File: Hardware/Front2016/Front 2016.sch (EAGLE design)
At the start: 182 parts

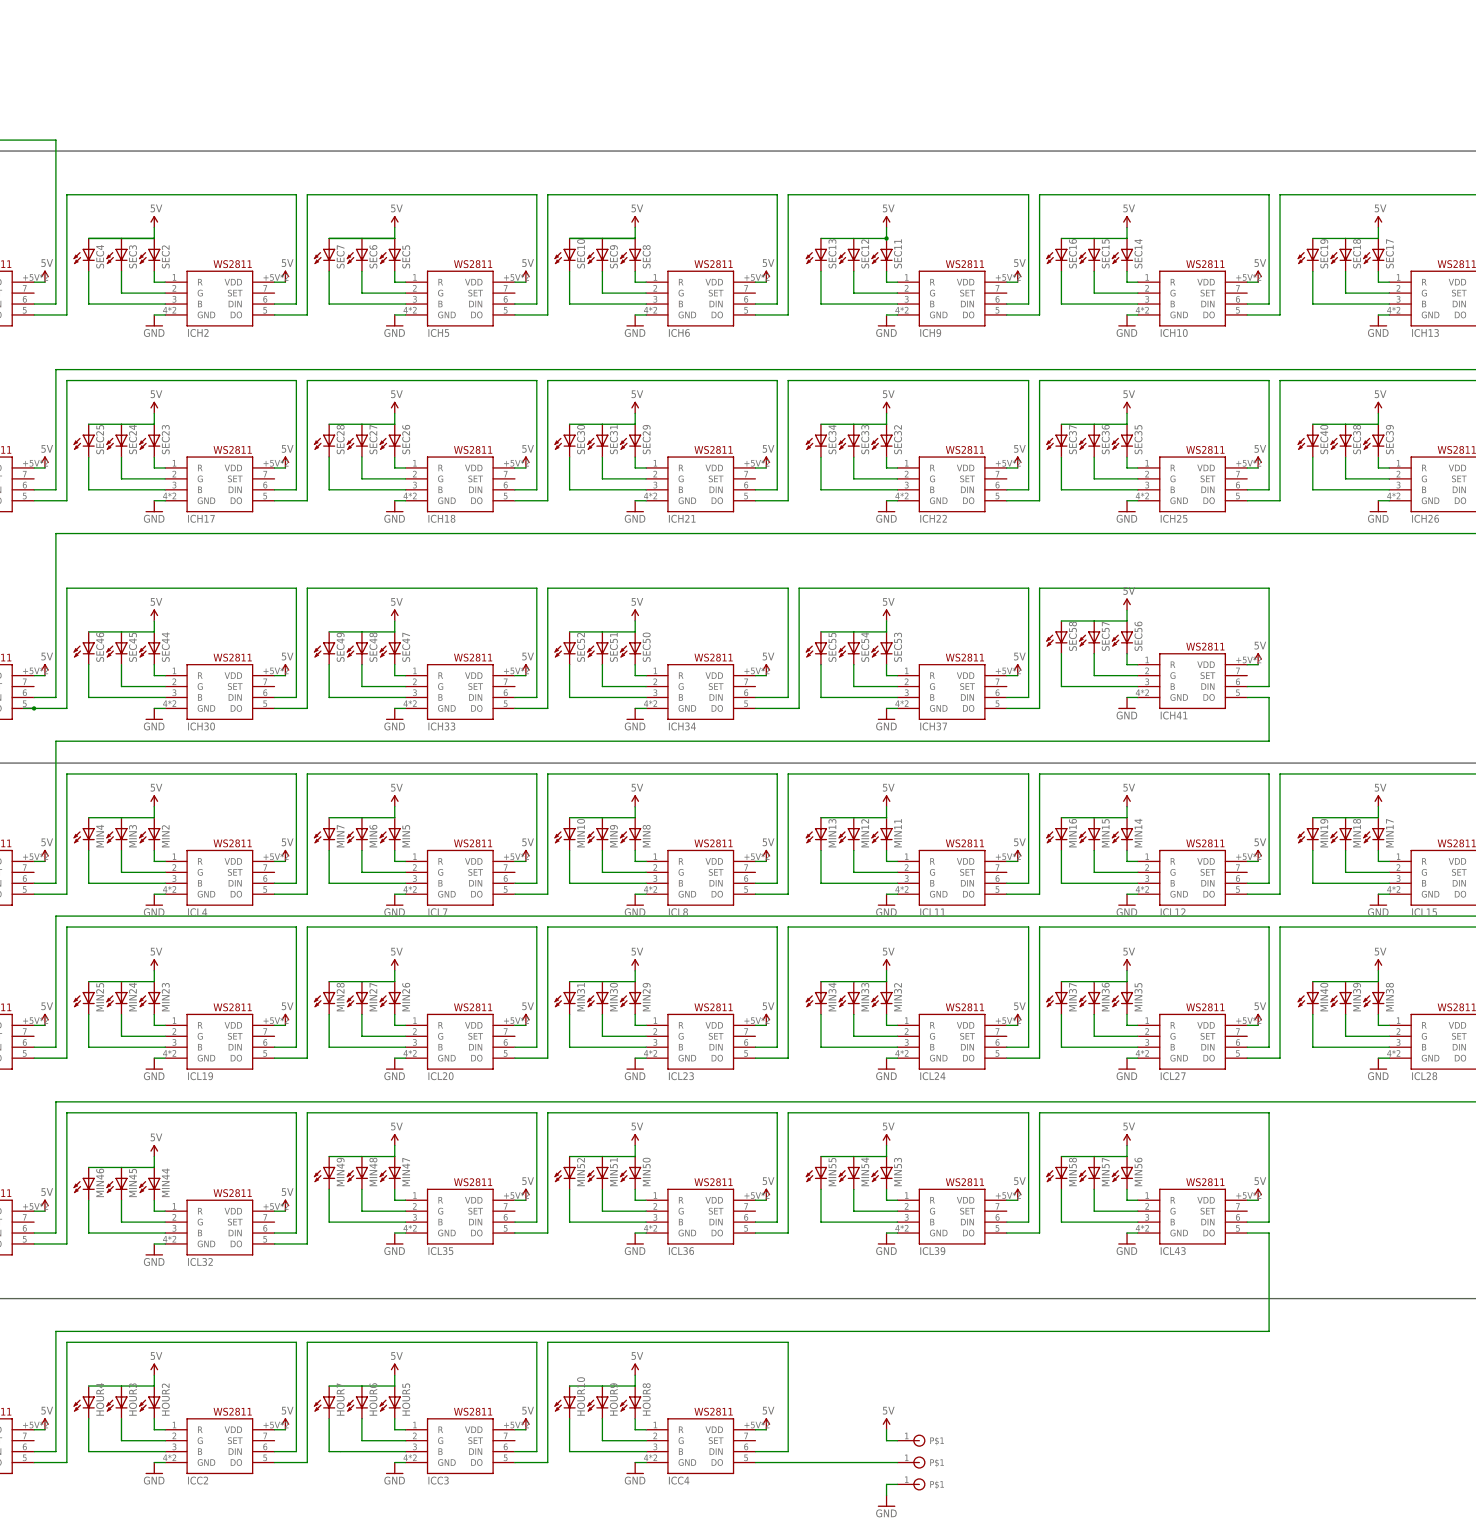
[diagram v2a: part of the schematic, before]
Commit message: 100% routed, Updated the TIMEARC_KEEPOUT footprint to include the 4 drill holes
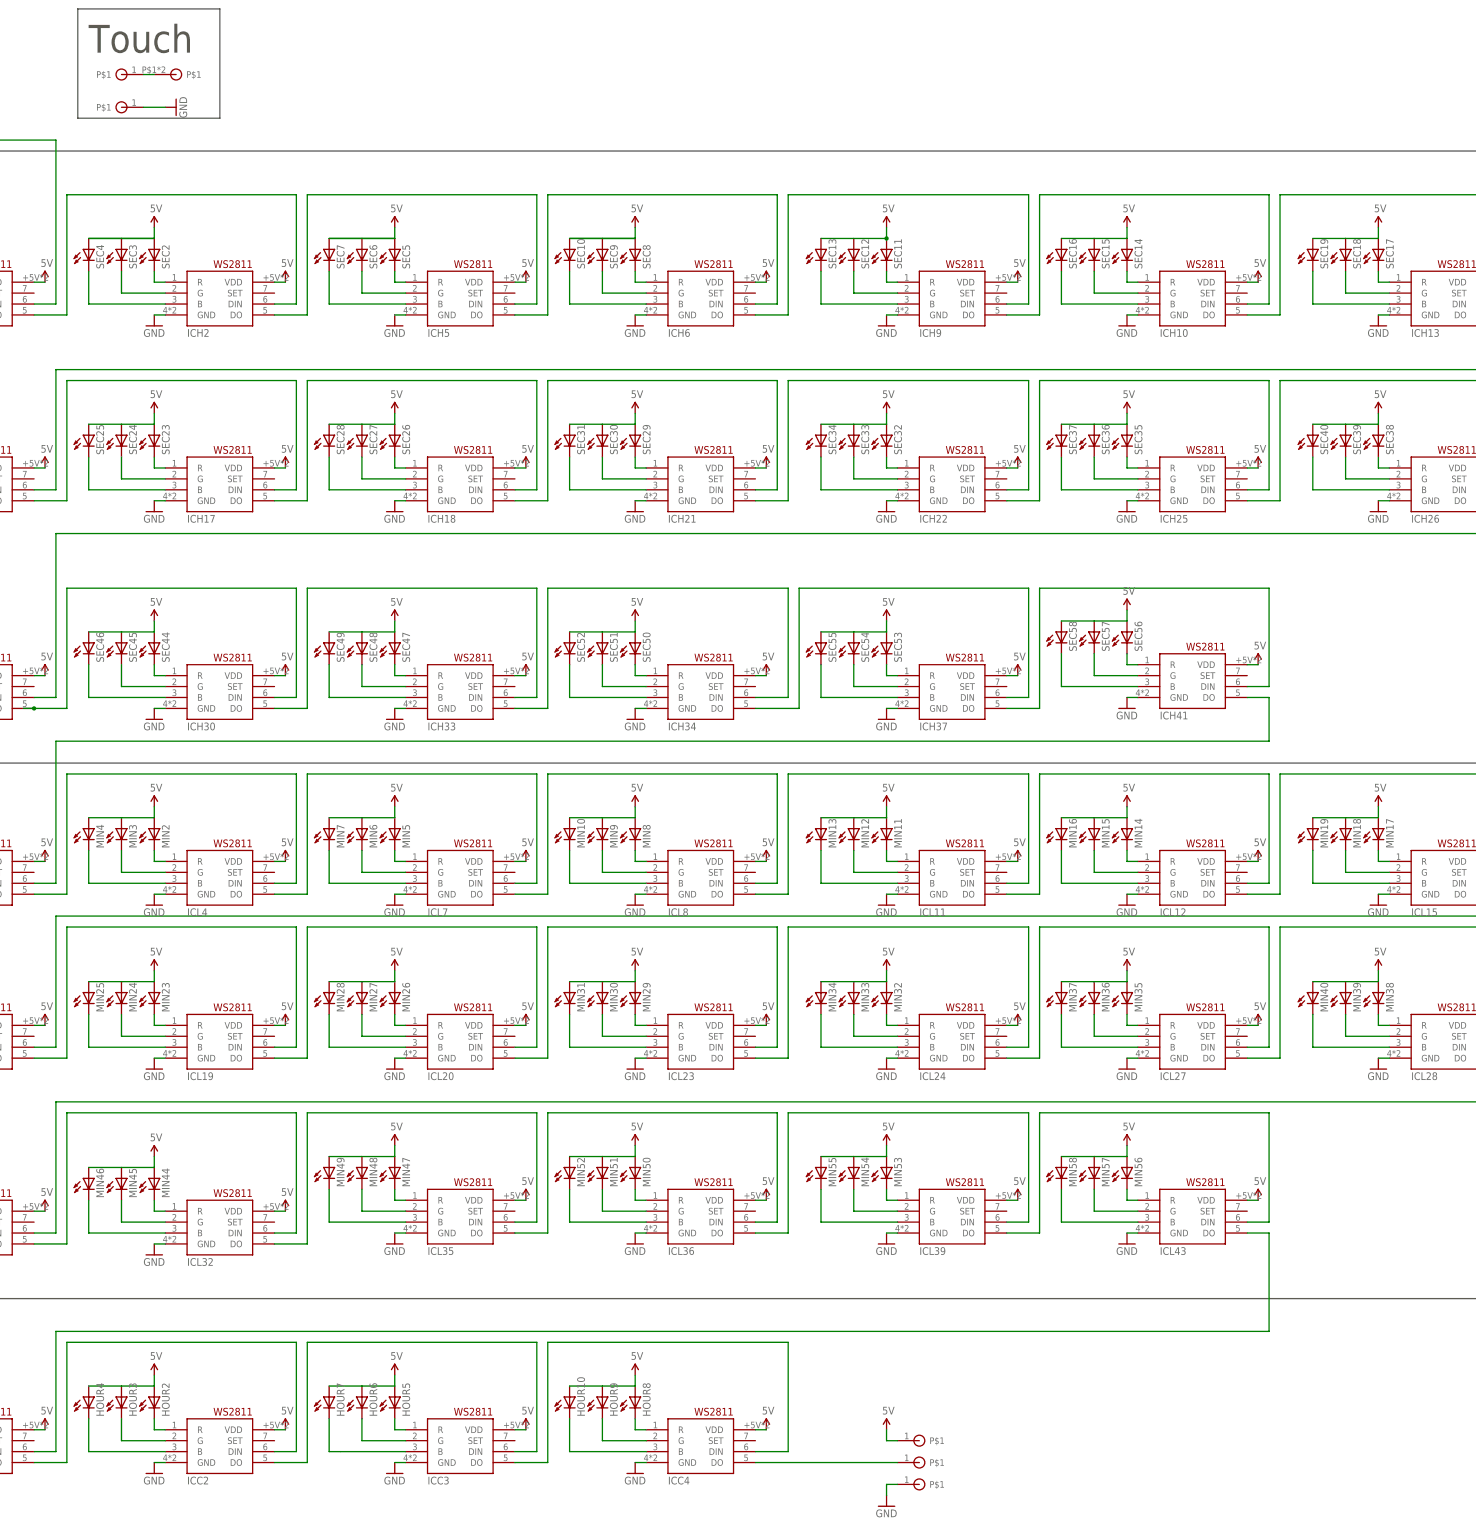
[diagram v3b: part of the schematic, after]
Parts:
- added GND48, TOUCH: SOLDER_PAD, timearc:SOLDER_PAD
- added U$2: TOUCH_PAD_LARGE, timearc:TOUCH_PAD_LARGE
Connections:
- new net TOUCH: TOUCH.P$1, U$2.P$1
- net GND: now also GND48.P$1
- net N$17: now also SEC39.C; no longer SEC38.C
- net N$36: now also SEC30.C; no longer SEC31.C
- net N$37: now also SEC31.C; no longer SEC30.C
- net N$47: now also SEC38.C; no longer SEC39.C
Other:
- note added: "Touch"
- moved on the sheet: SEC30, SEC31, SEC38, SEC39
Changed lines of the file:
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@@
 <part name="SUPPLY90" library="SparkFun-Aesthetics" deviceset="5V" device=""/>
 <part name="GND47" library="SparkFun-Aesthetics" deviceset="GND" device=""/>
+<part name="TOUCH" library="timearc" deviceset="SOLDER_PAD" device=""/>
+<part name="U$2" library="timearc" deviceset="TOUCH_PAD_LARGE" device=""/>
+<part name="GND48" library="timearc" deviceset="SOLDER_PAD" device=""/>
+<part name="GND49" library="SparkFun-Aesthetics" deviceset="GND" device=""/>
 </parts>
 <sheets>
@@
 <wire x1="0" y1="0" x2="419.1" y2="0" width="0.1524" layer="97"/>
 <wire x1="419.1" y1="0" x2="419.1" y2="63.5" width="0.1524" layer="97"/>
+<text x="68.58" y="353.06" size="6.4516" layer="97">Touch</text>
+<wire x1="66.04" y1="363.22" x2="66.04" y2="337.82" width="0.1524" layer="97"/>
+<wire x1="66.04" y1="337.82" x2="99.06" y2="337.82" width="0.1524" layer="97"/>
+<wire x1="99.06" y1="337.82" x2="99.06" y2="363.22" width="0.1524" layer="97"/>
+<wire x1="99.06" y1="363.22" x2="66.04" y2="363.22" width="0.1524" layer="97"/>
 </plain>
 <instances>
@@
 <instance part="SEC28" gate="G$1" x="124.46" y="264.16"/>
 <instance part="SEC29" gate="G$1" x="195.58" y="264.16"/>
-<instance part="SEC30" gate="G$1" x="180.34" y="264.16"/>
-<instance part="SEC31" gate="G$1" x="187.96" y="264.16"/>
+<instance part="SEC30" gate="G$1" x="187.96" y="264.16"/>
+<instance part="SEC31" gate="G$1" x="180.34" y="264.16"/>
 <instance part="SEC32" gate="G$1" x="254" y="264.16"/>
 <instance part="SEC33" gate="G$1" x="246.38" y="264.16"/>
@@
 <instance part="SEC36" gate="G$1" x="302.26" y="264.16"/>
 <instance part="SEC37" gate="G$1" x="294.64" y="264.16"/>
-<instance part="SEC38" gate="G$1" x="360.68" y="264.16"/>
-<instance part="SEC39" gate="G$1" x="368.3" y="264.16"/>
+<instance part="SEC38" gate="G$1" x="368.3" y="264.16"/>
+<instance part="SEC39" gate="G$1" x="360.68" y="264.16"/>
 <instance part="SEC40" gate="G$1" x="353.06" y="264.16"/>
 <instance part="SEC41" gate="G$1" x="27.94" y="215.9"/>
@@
 <instance part="SUPPLY90" gate="G$1" x="254" y="33.02"/>
 <instance part="GND47" gate="1" x="254" y="15.24"/>
+<instance part="TOUCH" gate="A" x="76.2" y="347.98" rot="R270"/>
+<instance part="U$2" gate="G$1" x="88.9" y="347.98" rot="R90"/>
+<instance part="GND48" gate="A" x="76.2" y="340.36" rot="R270"/>
+<instance part="GND49" gate="1" x="88.9" y="340.36" rot="R90"/>
 </instances>
 <busses>
@@
 <pinref part="GND46" gate="A" pin="P$1"/>
 <wire x1="254" y1="20.32" x2="256.54" y2="20.32" width="0.1524" layer="91"/>
+</segment>
+<segment>
+<pinref part="GND49" gate="1" pin="GND"/>
+<pinref part="GND48" gate="A" pin="P$1"/>
+<wire x1="86.36" y1="340.36" x2="81.28" y2="340.36" width="0.1524" layer="91"/>
 </segment>
 </net>
@@
 </segment>
 <segment>
-<pinref part="SEC30" gate="G$1" pin="A"/>
-<pinref part="SEC31" gate="G$1" pin="A"/>
-<wire x1="180.34" y1="266.7" x2="187.96" y2="266.7" width="0.1524" layer="91"/>
 <pinref part="SEC29" gate="G$1" pin="A"/>
-<wire x1="187.96" y1="266.7" x2="195.58" y2="266.7" width="0.1524" layer="91"/>
 <pinref part="SUPPLY55" gate="G$1" pin="5V"/>
 <wire x1="195.58" y1="266.7" x2="195.58" y2="269.24" width="0.1524" layer="91"/>
+<pinref part="SEC31" gate="G$1" pin="A"/>
+<pinref part="SEC30" gate="G$1" pin="A"/>
+<wire x1="180.34" y1="266.7" x2="187.96" y2="266.7" width="0.1524" layer="91"/>
+<wire x1="187.96" y1="266.7" x2="195.58" y2="266.7" width="0.1524" layer="91"/>
 </segment>
 <segment>
@@
 </segment>
 <segment>
-<pinref part="SEC40" gate="G$1" pin="A"/>
-<pinref part="SEC38" gate="G$1" pin="A"/>
-<wire x1="353.06" y1="266.7" x2="360.68" y2="266.7" width="0.1524" layer="91"/>
-<pinref part="SEC39" gate="G$1" pin="A"/>
-<wire x1="360.68" y1="266.7" x2="368.3" y2="266.7" width="0.1524" layer="91"/>
-<pinref part="SUPPLY58" gate="G$1" pin="5V"/>
-<wire x1="368.3" y1="266.7" x2="368.3" y2="269.24" width="0.1524" layer="91"/>
-</segment>
-<segment>
 <pinref part="SEC43" gate="G$1" pin="A"/>
 <pinref part="SEC42" gate="G$1" pin="A"/>
@@
 <wire x1="195.58" y1="43.18" x2="195.58" y2="45.72" width="0.1524" layer="91"/>
 </segment>
+<segment>
+<pinref part="SEC40" gate="G$1" pin="A"/>
+<pinref part="SEC39" gate="G$1" pin="A"/>
+<wire x1="353.06" y1="266.7" x2="360.68" y2="266.7" width="0.1524" layer="91"/>
+<pinref part="SEC38" gate="G$1" pin="A"/>
+<wire x1="360.68" y1="266.7" x2="368.3" y2="266.7" width="0.1524" layer="91"/>
+<pinref part="SUPPLY58" gate="G$1" pin="5V"/>
+<wire x1="368.3" y1="266.7" x2="368.3" y2="269.24" width="0.1524" layer="91"/>
+</segment>
 </net>
 <net name="N$3" class="0">
@@
 <net name="N$36" class="0">
 <segment>
+<pinref part="ICH21" gate="G$1" pin="G"/>
+<wire x1="187.96" y1="254" x2="198.12" y2="254" width="0.1524" layer="91"/>
+<pinref part="SEC30" gate="G$1" pin="C"/>
+<wire x1="187.96" y1="254" x2="187.96" y2="259.08" width="0.1524" layer="91"/>
+</segment>
+</net>
+<net name="N$37" class="0">
+<segment>
+<pinref part="ICH21" gate="G$1" pin="B"/>
+<wire x1="180.34" y1="251.46" x2="198.12" y2="251.46" width="0.1524" layer="91"/>
 <pinref part="SEC31" gate="G$1" pin="C"/>
-<pinref part="ICH21" gate="G$1" pin="G"/>
-<wire x1="187.96" y1="259.08" x2="187.96" y2="254" width="0.1524" layer="91"/>
-<wire x1="187.96" y1="254" x2="198.12" y2="254" width="0.1524" layer="91"/>
-</segment>
-</net>
-<net name="N$37" class="0">
-<segment>
-<pinref part="SEC30" gate="G$1" pin="C"/>
-<pinref part="ICH21" gate="G$1" pin="B"/>
-<wire x1="180.34" y1="259.08" x2="180.34" y2="251.46" width="0.1524" layer="91"/>
-<wire x1="180.34" y1="251.46" x2="198.12" y2="251.46" width="0.1524" layer="91"/>
+<wire x1="180.34" y1="251.46" x2="180.34" y2="259.08" width="0.1524" layer="91"/>
 </segment>
 </net>
@@
 <net name="N$47" class="0">
 <segment>
-<pinref part="SEC39" gate="G$1" pin="C"/>
-<wire x1="368.3" y1="259.08" x2="368.3" y2="256.54" width="0.1524" layer="91"/>
 <pinref part="ICH26" gate="G$1" pin="R"/>
 <wire x1="368.3" y1="256.54" x2="370.84" y2="256.54" width="0.1524" layer="91"/>
+<pinref part="SEC38" gate="G$1" pin="C"/>
+<wire x1="368.3" y1="256.54" x2="368.3" y2="259.08" width="0.1524" layer="91"/>
 </segment>
 </net>
 <net name="N$17" class="0">
 <segment>
-<pinref part="SEC38" gate="G$1" pin="C"/>
 <pinref part="ICH26" gate="G$1" pin="G"/>
-<wire x1="360.68" y1="259.08" x2="360.68" y2="254" width="0.1524" layer="91"/>
 <wire x1="360.68" y1="254" x2="370.84" y2="254" width="0.1524" layer="91"/>
+<pinref part="SEC39" gate="G$1" pin="C"/>
+<wire x1="360.68" y1="254" x2="360.68" y2="259.08" width="0.1524" layer="91"/>
 </segment>
 </net>
@@
 </segment>
 </net>
+<net name="TOUCH" class="0">
+<segment>
+<pinref part="TOUCH" gate="A" pin="P$1"/>
+<wire x1="81.28" y1="347.98" x2="83.82" y2="347.98" width="0.1524" layer="91"/>
+<pinref part="U$2" gate="G$1" pin="P$1"/>
+</segment>
+</net>
 <net name="N$164" class="0">
 <segment>
+<pinref part="ICC4" gate="G$1" pin="DO"/>
 <pinref part="DOUT" gate="A" pin="P$1"/>
-<wire x1="256.54" y1="25.4" x2="223.52" y2="25.4" width="0.1524" layer="91"/>
-<pinref part="ICC4" gate="G$1" pin="DO"/>
-</segment>
-</net>
+<wire x1="223.52" y1="25.4" x2="256.54" y2="25.4" width="0.1524" layer="91"/>
+</segment>
+</net>
